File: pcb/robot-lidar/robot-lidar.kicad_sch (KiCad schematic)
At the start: 37 parts, among them J2 YLIDAR X4, J3 Jack-DC, J5 Conn_02x03_Odd_Even, J7 Conn_ARM_SWD_TagConnect_TC2030, SW1 SW_SPST, U1 STM32F429VETx, U2 LM317-3.3_SOT-223, U2 MPU-6050, U4 MX1508, U5 MX1508, Y1 Crystal

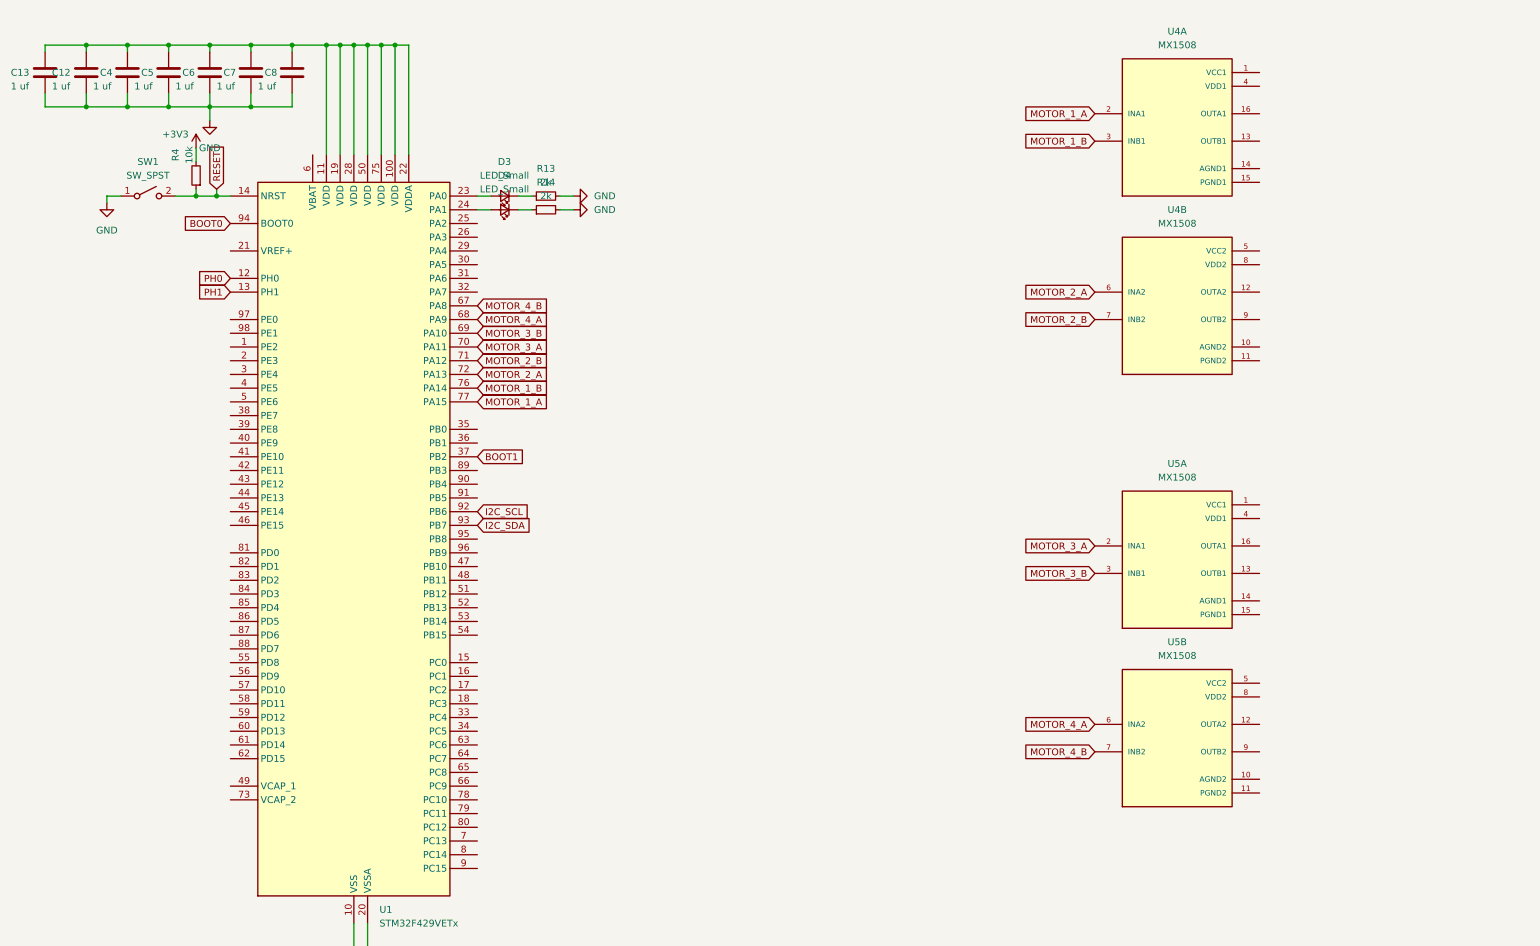
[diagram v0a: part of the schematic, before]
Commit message: add motor pin
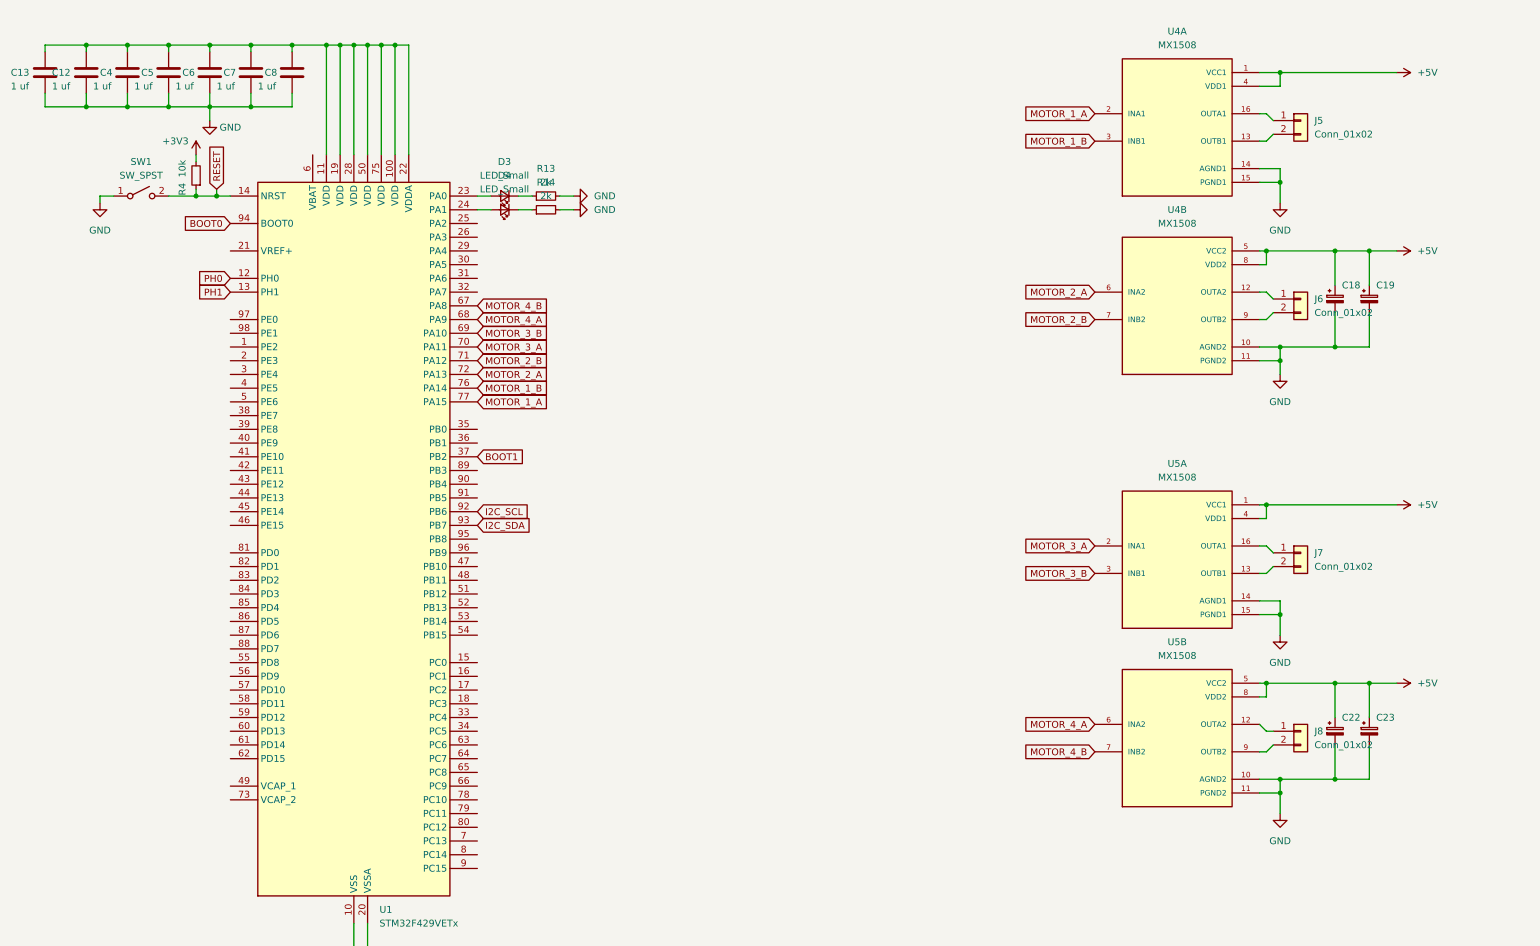
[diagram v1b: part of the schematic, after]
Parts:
- added C18, C19, C22, C23: C_Polarized_Small, Capacitor_SMD:CP_Elec_6.3x4.9, symbol Device:C_Polarized_Small
- added J5, J6, J7, J8: Conn_01x02, Connector_PinSocket_2.54mm:PinSocket_1x02_P2.54mm_Vertical, symbol Connector_Generic:Conn_01x02
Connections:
- net +5V: now also U4.1 (VCC1), U4.4 (VDD1), U4.5 (VCC2), U4.8 (VDD2), U5.1 (VCC1), U5.4 (VDD1), U5.5 (VCC2), U5.8 (VDD2), C18.1, C19.1, C22.1, C23.1
- net GND: now also U4.10 (AGND2), U4.11 (PGND2), U4.14 (AGND1), U4.15 (PGND1), U5.10 (AGND2), U5.11 (PGND2), U5.14 (AGND1), U5.15 (PGND1), C18.2, C19.2, C22.2, C23.2
- net at U5.12 (OUTA2): now also J8.1 (Pin_1)
- net at U5.9 (OUTB2): now also J8.2 (Pin_2)
- net at U4.12 (OUTA2): now also J6.1 (Pin_1)
- net at U4.9 (OUTB2): now also J6.2 (Pin_2)
- net at U5.13 (OUTB1): now also J7.2 (Pin_2)
- net at U5.16 (OUTA1): now also J7.1 (Pin_1)
- net at U4.13 (OUTB1): now also J5.2 (Pin_2)
- net at U4.16 (OUTA1): now also J5.1 (Pin_1)
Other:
- moved on the sheet: SW1

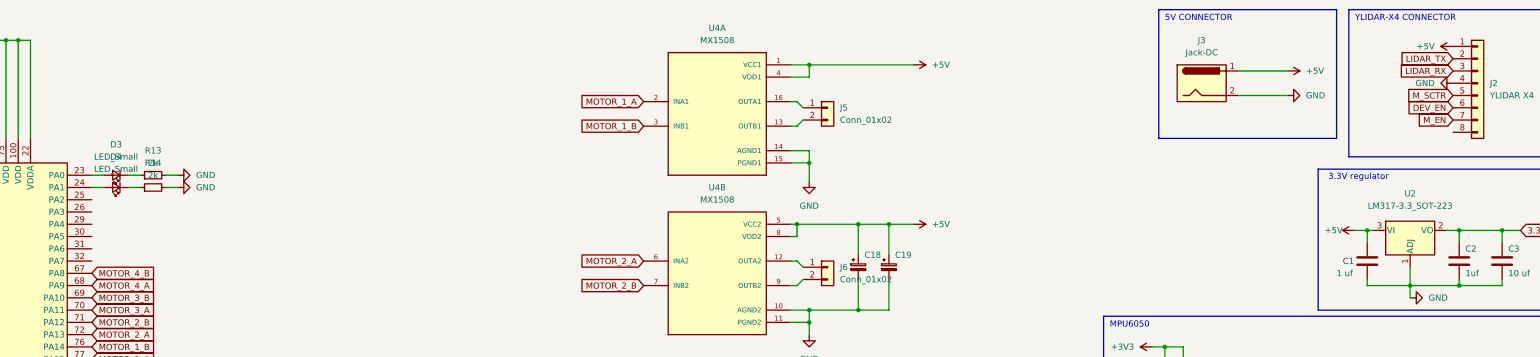
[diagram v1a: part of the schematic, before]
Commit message: add pcb edge cut
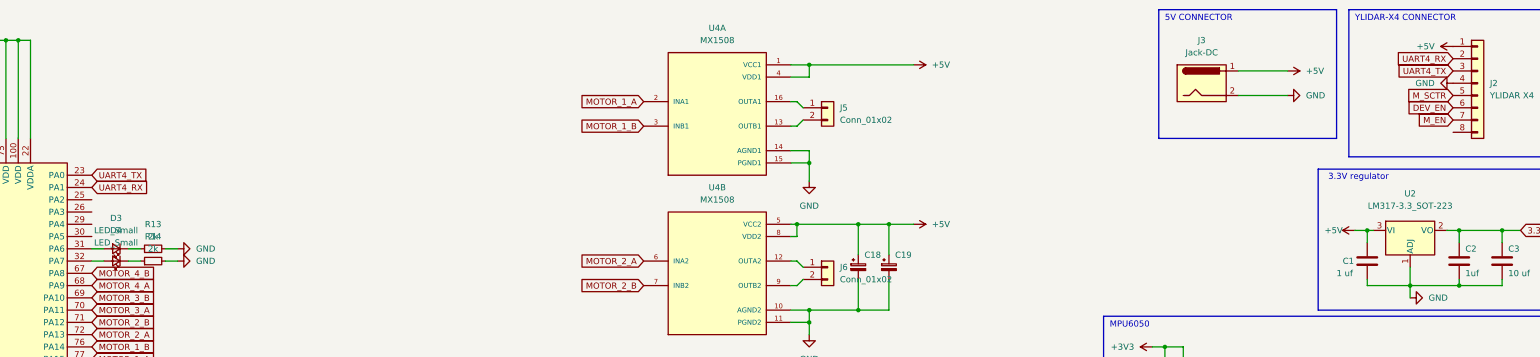
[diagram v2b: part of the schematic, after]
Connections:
- net at D4.2 (A): now also U1.32 (PA7); no longer U1.24 (PA1)
- net at D3.2 (A): now also U1.31 (PA6); no longer U1.23 (PA0)
- net LIDAR_RX renamed UART4_TX
- net UART4_TX: now also U1.23 (PA0)
- net LIDAR_TX renamed UART4_RX
- net UART4_RX: now also U1.24 (PA1)

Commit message: 3.3 wiring
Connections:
- net 3.3V is gone; now on net +3V3: C2.1, C3.1, U2.2 (VO)
- net +3V3: now also C12.1, C13.1, C4.1, C5.1, C6.1, C7.1, C8.1, U1.100 (VDD), U1.11 (VDD), U1.19 (VDD), U1.22 (VDDA), U1.28 (VDD), U1.50 (VDD), U1.75 (VDD)
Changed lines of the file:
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@@
   (junction (at 82.55 21.59) (diameter 0) (color 0 0 0 0)
   )
+  (junction (at 20.32 21.59) (diameter 0) (color 0 0 0 0)
+  )
   (junction (at 265.43 59.69) (diameter 0) (color 0 0 0 0)
   )
@@
     )
   )
-  (global_label "3.3V" (shape input) (at 396.24 60.96 0) (fields_autoplaced)
-    (effects (font (size 1.27 1.27)) (justify left))
-    (property "Intersheetrefs" "${INTERSHEET_REFS}" (at 402.7655 60.8806 0)
-      (effects (font (size 1.27 1.27)) (justify left) hide)
-    )
-  )
   (global_label "PH1" (shape input) (at 143.51 261.62 90) (fields_autoplaced)
     (effects (font (size 1.27 1.27)) (justify left))
@@
     )
   )
+  (symbol (lib_id "power:+3V3") (at 396.24 60.96 270) (unit 1)
+    (in_bom yes) (on_board yes) (dnp no) (fields_autoplaced)
+    (property "Reference" "#PWR032" (at 392.43 60.96 0)
+      (effects (font (size 1.27 1.27)) hide)
+    )
+    (property "Value" "+3V3" (at 400.05 60.96 90)
+      (effects (font (size 1.27 1.27)) (justify left))
+    )
+    (property "Footprint" "" (at 396.24 60.96 0)
+      (effects (font (size 1.27 1.27)) hide)
+    )
+    (property "Datasheet" "" (at 396.24 60.96 0)
+      (effects (font (size 1.27 1.27)) hide)
+    )
+    (pin "1")
+    (instances
+      (project "robot-lidar"
+        (path "/cb10bbf7-c2c1-4a0d-8947-ad707931d83b"
+          (reference "#PWR032") (unit 1)
+        )
+      )
+    )
+  )
   (symbol (lib_id "power:GND") (at 382.27 30.48 270) (unit 1)
     (in_bom yes) (on_board yes) (dnp no) (fields_autoplaced)
@@
         )
       )
+    )
+  )
+  (symbol (lib_id "power:+3V3") (at 20.32 21.59 0) (unit 1)
+    (in_bom yes) (on_board yes) (dnp no) (fields_autoplaced)
+    (property "Reference" "#PWR033" (at 20.32 25.4 0)
+      (effects (font (size 1.27 1.27)) hide)
+    )
+    (property "Value" "+3V3" (at 20.32 16.51 0)
+      (effects (font (size 1.27 1.27)))
+    )
+    (property "Footprint" "" (at 20.32 21.59 0)
+      (effects (font (size 1.27 1.27)) hide)
+    )
+    (property "Datasheet" "" (at 20.32 21.59 0)
+      (effects (font (size 1.27 1.27)) hide)
+    )
+    (pin "1")
+    (instances
+      (project "robot-lidar"
+        (path "/cb10bbf7-c2c1-4a0d-8947-ad707931d83b"
+          (reference "#PWR033") (unit 1)
+        )
+      )

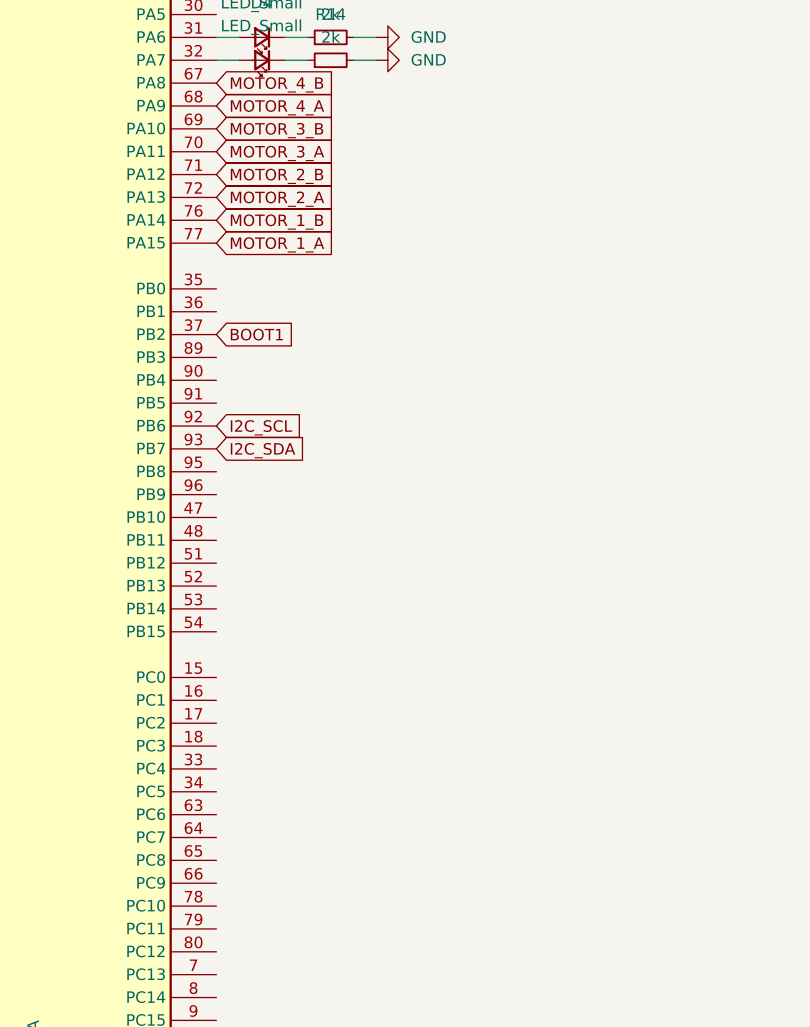
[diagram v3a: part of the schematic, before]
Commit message: wiring lidar
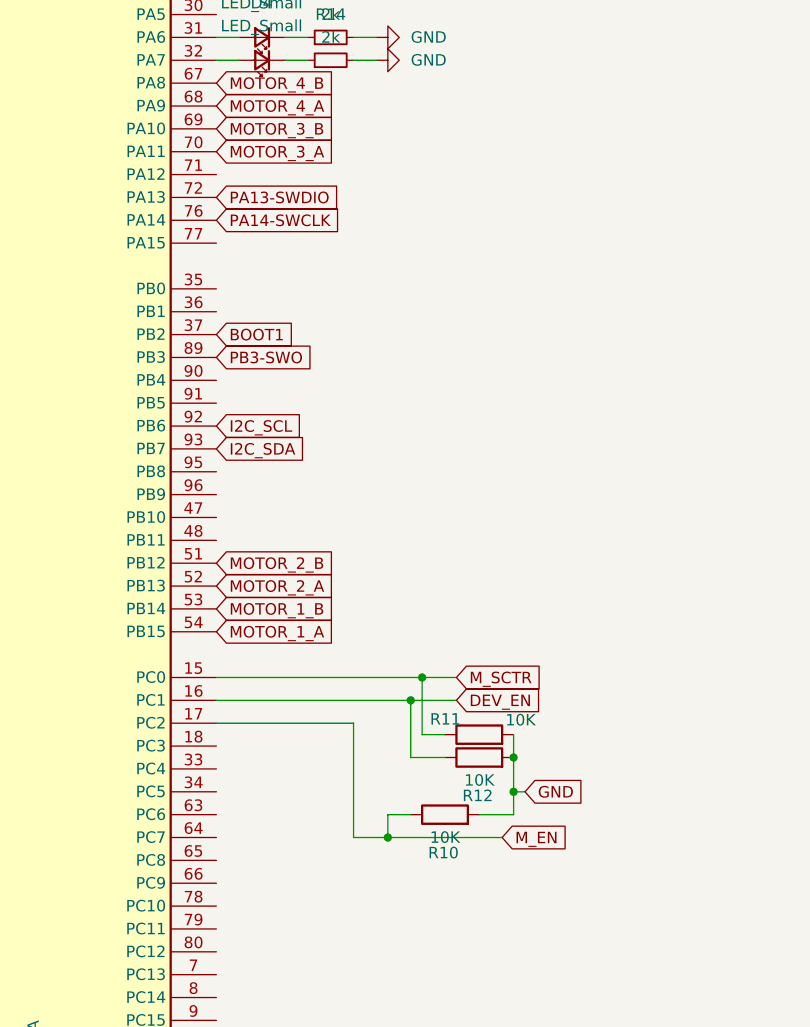
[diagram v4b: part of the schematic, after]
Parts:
- added R10, R11, R12: 10K, Resistor_SMD:R_0603_1608Metric, symbol Device:R
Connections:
- net DEV_EN: now also U1.16 (PC1), R12.1
- net GND: now also R10.2, R11.2, R12.2
- net MOTOR_1_A: now also U1.54 (PB15); no longer U1.77 (PA15)
- net MOTOR_1_B: now also U1.53 (PB14); no longer U1.76 (PA14)
- net MOTOR_2_A: now also U1.52 (PB13); no longer U1.72 (PA13)
- net MOTOR_2_B: now also U1.51 (PB12); no longer U1.71 (PA12)
- net M_EN: now also U1.17 (PC2), R10.1
- net M_SCTR: now also U1.15 (PC0), R11.1
- net PA13-SWDIO: now also U1.72 (PA13)
- net PA14-SWCLK: now also U1.76 (PA14)
- net PB3-SWO: now also U1.89 (PB3)

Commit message: add linkit
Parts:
- added J10, J9: Conn_01x18, symbol Connector_Generic:Conn_01x18
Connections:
- net +3V3: now also J9.12 (Pin_12)
- net +5V: now also J9.14 (Pin_14)
- net UART5_TX: now reaches U1.80 (PC12)
- net UART5_TX: now also J10.14 (Pin_14)
- net UART5_RX: now reaches U1.83 (PD2)
- net UART5_RX: now also J10.13 (Pin_13)
- new net USB_DM: J9.8 (Pin_8)
- new net USB_DP: J9.7 (Pin_7)
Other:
- note added: "UART_MAPPING_MCU_MT"
- moved on the sheet: R11, R12
